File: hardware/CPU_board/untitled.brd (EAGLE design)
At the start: 128.9 x 94.9 mm, 71 parts, among them IC1 MAX232ECWE, IC2 MAX232ECWE, IC3 AM29F040J, IC4 74HCT138D, IC5 LM2596S, IC6 74245SSOP, IC7 74245SSOP, IC8 74245SSOP, J2 POWER_JACKSLT, U1 AS6C4008-55SIN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

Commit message: Minor changes
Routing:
- net GND: track 94.2 -> 95.9 mm
- net SLCT: track 92.5 -> 91.0 mm
- net PE: track 88.7 -> 87.2 mm
- net BUSY: track 85.0 -> 83.5 mm
- net /ERR: track 65.9 -> 64.4 mm
- net /ACK: track 82.2 -> 80.7 mm
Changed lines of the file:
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@@
 <contactref element="IC8" pad="4"/>
 <wire x1="72.707" y1="50.038" x2="72.707" y2="51.244" width="0.3048" layer="1"/>
-<wire x1="72.707" y1="51.244" x2="72.7202" y2="51.2572" width="0.3048" layer="1"/>
 <wire x1="72.707" y1="50.038" x2="72.707" y2="48.958" width="0.3048" layer="1"/>
 <wire x1="72.707" y1="48.958" x2="72.6948" y2="48.9458" width="0.3048" layer="1"/>
@@
 <contactref element="C26" pad="2"/>
 <contactref element="C27" pad="2"/>
+<wire x1="72.707" y1="51.244" x2="72.707" y2="51.372" width="0.2667" layer="1"/>
+<wire x1="72.707" y1="51.372" x2="72.4408" y2="51.6382" width="0.2667" layer="1"/>
+<wire x1="72.4408" y1="51.6382" x2="71.2724" y2="51.6382" width="0.2667" layer="1"/>
+<wire x1="71.2724" y1="51.6382" x2="71.247" y2="51.6636" width="0.2667" layer="1"/>
 </signal>
 <signal name="5V">
@@
 <wire x1="27.305" y1="69.85" x2="31.3182" y2="69.85" width="0.8128" layer="1"/>
 <contactref element="JP7" pad="1"/>
-<wire x1="45.2558" y1="85.9102" x2="59.69" y2="85.9102" width="1.0668" layer="1"/>
+<wire x1="45.2558" y1="85.9102" x2="59.69" y2="85.9102" width="1.6764" layer="1"/>
 <wire x1="59.69" y1="85.9102" x2="59.69" y2="88.265" width="1.0668" layer="1"/>
 <contactref element="C22" pad="+"/>
@@
 <contactref element="JP9" pad="4"/>
 <contactref element="IC8" pad="5"/>
-<wire x1="70.802" y1="56.642" x2="70.802" y2="60.3118" width="0.3048" layer="1"/>
-<wire x1="70.802" y1="60.3118" x2="71.6534" y2="61.1632" width="0.3048" layer="1"/>
-<wire x1="71.6534" y1="61.1632" x2="89.7636" y2="61.1632" width="0.3048" layer="1"/>
+<wire x1="70.802" y1="56.642" x2="70.802" y2="57.7718" width="0.3048" layer="1"/>
+<wire x1="70.802" y1="57.7718" x2="74.1934" y2="61.1632" width="0.3048" layer="1"/>
+<wire x1="74.1934" y1="61.1632" x2="89.7636" y2="61.1632" width="0.3048" layer="1"/>
 <wire x1="89.7636" y1="61.1632" x2="102.0064" y2="73.406" width="0.3048" layer="1"/>
 <wire x1="93.98" y1="76.2" x2="93.98" y2="78.105" width="0.3048" layer="1"/>
@@
 <contactref element="JP9" pad="19"/>
 <contactref element="IC8" pad="9"/>
-<wire x1="68.262" y1="56.642" x2="68.262" y2="61.2262" width="0.3048" layer="1"/>
-<wire x1="68.262" y1="61.2262" x2="70.6374" y2="63.6016" width="0.3048" layer="1"/>
-<wire x1="70.6374" y1="63.6016" x2="88.7984" y2="63.6016" width="0.3048" layer="1"/>
+<wire x1="68.262" y1="56.642" x2="68.262" y2="58.6862" width="0.3048" layer="1"/>
+<wire x1="68.262" y1="58.6862" x2="73.1774" y2="63.6016" width="0.3048" layer="1"/>
+<wire x1="73.1774" y1="63.6016" x2="88.7984" y2="63.6016" width="0.3048" layer="1"/>
 <wire x1="88.7984" y1="63.6016" x2="99.0092" y2="73.8124" width="0.3048" layer="1"/>
 <wire x1="99.0092" y1="73.8124" x2="99.0092" y2="85.0138" width="0.3048" layer="1"/>
@@
 <contactref element="JP9" pad="21"/>
 <contactref element="IC8" pad="8"/>
-<wire x1="68.897" y1="56.642" x2="68.897" y2="60.9976" width="0.3048" layer="1"/>
-<wire x1="68.897" y1="60.9976" x2="70.8914" y2="62.992" width="0.3048" layer="1"/>
-<wire x1="70.8914" y1="62.992" x2="89.027" y2="62.992" width="0.3048" layer="1"/>
+<wire x1="68.897" y1="56.642" x2="68.897" y2="58.4576" width="0.3048" layer="1"/>
+<wire x1="68.897" y1="58.4576" x2="73.4314" y2="62.992" width="0.3048" layer="1"/>
+<wire x1="73.4314" y1="62.992" x2="89.027" y2="62.992" width="0.3048" layer="1"/>
 <wire x1="89.027" y1="62.992" x2="99.6188" y2="73.5838" width="0.3048" layer="1"/>
 <wire x1="99.6188" y1="73.5838" x2="99.6188" y2="85.2678" width="0.3048" layer="1"/>
@@
 <contactref element="JP9" pad="23"/>
 <contactref element="IC8" pad="7"/>
-<wire x1="69.532" y1="56.642" x2="69.532" y2="60.769" width="0.3048" layer="1"/>
-<wire x1="69.532" y1="60.769" x2="71.1454" y2="62.3824" width="0.3048" layer="1"/>
-<wire x1="71.1454" y1="62.3824" x2="89.2556" y2="62.3824" width="0.3048" layer="1"/>
+<wire x1="69.532" y1="56.642" x2="69.532" y2="58.229" width="0.3048" layer="1"/>
+<wire x1="69.532" y1="58.229" x2="73.6854" y2="62.3824" width="0.3048" layer="1"/>
+<wire x1="73.6854" y1="62.3824" x2="89.2556" y2="62.3824" width="0.3048" layer="1"/>
 <wire x1="89.2556" y1="62.3824" x2="100.2284" y2="73.3552" width="0.3048" layer="1"/>
 <wire x1="100.2284" y1="73.3552" x2="100.2284" y2="85.5218" width="0.3048" layer="1"/>
@@
 <contactref element="JP9" pad="25"/>
 <contactref element="IC8" pad="6"/>
-<wire x1="70.167" y1="56.642" x2="70.167" y2="60.5404" width="0.3048" layer="1"/>
-<wire x1="70.167" y1="60.5404" x2="71.3994" y2="61.7728" width="0.3048" layer="1"/>
-<wire x1="71.3994" y1="61.7728" x2="89.5096" y2="61.7728" width="0.3048" layer="1"/>
+<wire x1="70.167" y1="56.642" x2="70.167" y2="58.0004" width="0.3048" layer="1"/>
+<wire x1="70.167" y1="58.0004" x2="73.9394" y2="61.7728" width="0.3048" layer="1"/>
+<wire x1="73.9394" y1="61.7728" x2="89.5096" y2="61.7728" width="0.3048" layer="1"/>
 <wire x1="89.5096" y1="61.7728" x2="100.838" y2="73.1012" width="0.3048" layer="1"/>
 <wire x1="100.838" y1="73.1012" x2="100.838" y2="85.7758" width="0.3048" layer="1"/>

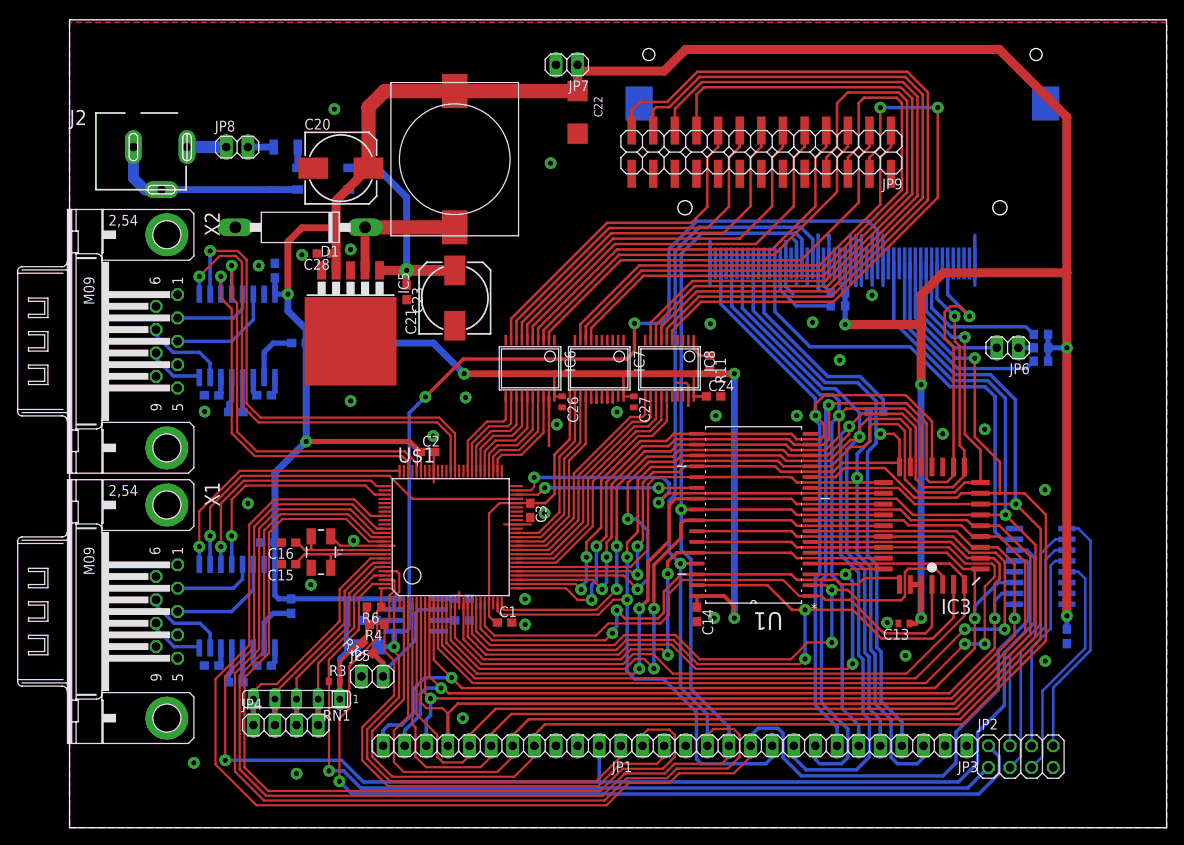
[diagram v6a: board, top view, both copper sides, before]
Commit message: Mounting holes added, board size adjusted
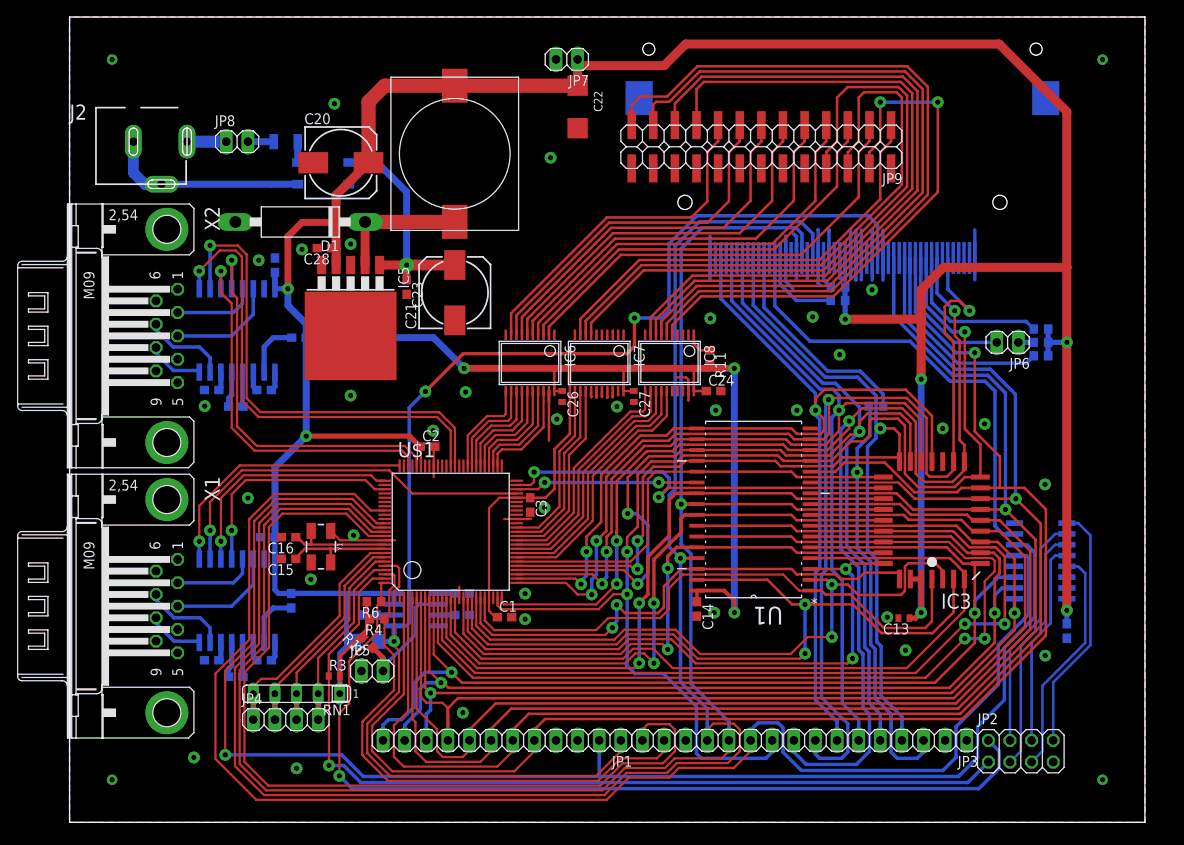
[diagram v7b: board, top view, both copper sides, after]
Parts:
- moved B1 0.64 mm to (29.8, 76.3)
- moved C2 0.64 mm to (42.1, 44.1)
- moved C20 0.64 mm to (31.9, 77.5)
- moved C24 0.64 mm to (75.7, 50.7)
- moved C28 0.64 mm to (29.9, 67.5)
- moved C9 0.64 mm to (26.9, 56.9)
- moved CON1 0.64 mm to (90.8, 85.1)
- moved F1 0.64 mm to (25.4, 80.0)
- moved IC3 0.64 mm to (101.3, 35.5)
- moved JP7 0.64 mm to (58.4, 89.6)
- moved JP8 0.64 mm to (19.7, 80.0)
- moved JP9 0.64 mm to (95.2, 78.1)
- moved R12 0.64 mm to (90.3, 61.3)
- moved R2 0.64 mm to (94.7, 48.9)
- moved R7 0.64 mm to (90.3, 62.9)
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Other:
- board size 128.9 x 94.9 mm -> 126.3 x 94.6 mm

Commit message: Dangling signals fixed
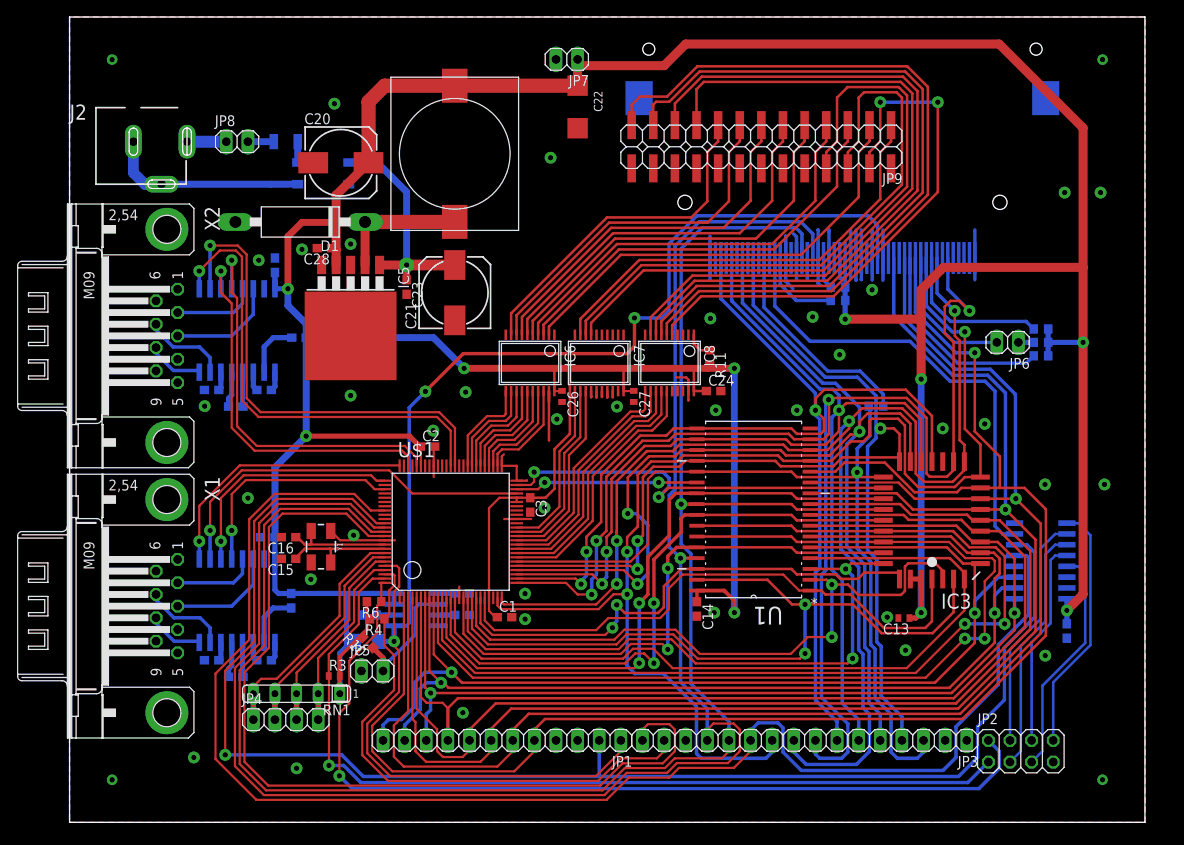
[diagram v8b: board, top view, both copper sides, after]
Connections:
- net 5V: now also U$1.45
- net GND: now also U$1.50, U$1.51
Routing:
- net GND: track 95.9 -> 102.1 mm, vias 33 -> 36
- net 5V: track 509.8 -> 515.7 mm
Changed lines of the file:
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@@
 <setting verticaltext="up"/>
 </settings>
-<grid distance="25" unitdist="mil" unit="mil" style="lines" multiple="1" display="no" altdistance="1" altunitdist="mm" altunit="mm"/>
+<grid distance="25" unitdist="mil" unit="mil" style="lines" multiple="1" display="no" altdistance="1" altunitdist="mil" altunit="mil"/>
 <layers>
 <layer number="1" name="Top" color="4" fill="1" visible="yes" active="yes"/>
@@
 <wire x1="72.4408" y1="52.2732" x2="71.2724" y2="52.2732" width="0.2667" layer="1"/>
 <wire x1="71.2724" y1="52.2732" x2="71.247" y2="52.2986" width="0.2667" layer="1"/>
+<via x="116.9162" y="73.9902" extent="1-16" drill="0.6" diameter="1.4224" shape="octagon"/>
+<via x="121.1326" y="73.9902" extent="1-16" drill="0.6" diameter="1.4224" shape="octagon"/>
+<via x="121.5898" y="39.7002" extent="1-16" drill="0.6" diameter="1.4224" shape="octagon"/>
+<contactref element="U$1" pad="50"/>
+<contactref element="U$1" pad="51"/>
+<wire x1="50.7802" y1="41.8876" x2="50.7802" y2="42.9824" width="0.2667" layer="1"/>
+<wire x1="50.7802" y1="42.9824" x2="51.0286" y2="43.2308" width="0.2667" layer="1"/>
+<wire x1="52.5302" y1="40.1376" x2="53.7012" y2="40.1376" width="0.2667" layer="1"/>
+<wire x1="53.7012" y1="40.1376" x2="53.7464" y2="40.1828" width="0.2667" layer="1"/>
+<wire x1="50.7802" y1="41.8876" x2="52.5302" y2="41.8876" width="0.2667" layer="1"/>
+<wire x1="52.5302" y1="41.8876" x2="52.5302" y2="40.1376" width="0.2667" layer="1"/>
 </signal>
 <signal name="5V">
@@
 <wire x1="117.1702" y1="24.892" x2="117.1702" y2="26.2636" width="0.6096" layer="16"/>
 <wire x1="117.1702" y1="24.892" x2="117.1702" y2="23.329" width="0.6096" layer="16"/>
-<wire x1="117.1702" y1="24.892" x2="117.1702" y2="56.388" width="1.0668" layer="1"/>
 <contactref element="R4" pad="2"/>
 <contactref element="R5" pad="2"/>
@@
 <wire x1="34.146159375" y1="21.733840625" x2="34.0741" y2="21.8059" width="0.2667" layer="1"/>
 <wire x1="31.75" y1="15.113" x2="31.75" y2="15.24" width="0.4064" layer="16"/>
-<via x="117.1702" y="56.388" extent="1-16" drill="0.6" diameter="1.4224" shape="octagon"/>
-<wire x1="114.9722" y1="56.388" x2="117.1702" y2="56.388" width="0.6096" layer="16"/>
+<via x="119.0752" y="56.388" extent="1-16" drill="0.6" diameter="1.4224" shape="octagon"/>
+<wire x1="114.9722" y1="56.388" x2="119.0752" y2="56.388" width="0.6096" layer="16"/>
 <contactref element="C20" pad="+"/>
 <wire x1="31.3182" y1="65.4812" x2="31.3182" y2="67.31" width="1.0668" layer="1"/>
@@
 <wire x1="41.2124" y1="44.1452" x2="41.1734" y2="44.1452" width="0.6096" layer="1"/>
 <via x="91.1216" y="59.1194" extent="1-16" drill="0.6" diameter="1.4224" shape="octagon"/>
-<wire x1="109.22" y1="91.44" x2="117.1702" y2="83.4898" width="1.0668" layer="1"/>
-<wire x1="117.1702" y1="56.388" x2="117.1702" y2="65.20024375" width="1.0668" layer="1"/>
-<wire x1="117.1702" y1="65.20024375" x2="117.1702" y2="83.4898" width="1.0668" layer="1"/>
+<wire x1="109.22" y1="91.44" x2="119.0752" y2="81.5848" width="1.0668" layer="1"/>
+<wire x1="119.0752" y1="56.388" x2="119.0752" y2="65.20024375" width="1.0668" layer="1"/>
+<wire x1="119.0752" y1="65.20024375" x2="119.0752" y2="81.5848" width="1.0668" layer="1"/>
 <wire x1="91.1216" y1="59.1194" x2="100.0506" y2="59.1194" width="1.0668" layer="1"/>
 <wire x1="100.0506" y1="59.1194" x2="100.0506" y2="52.07" width="1.0668" layer="1"/>
-<wire x1="117.1702" y1="65.20024375" x2="102.66524375" y2="65.20024375" width="1.0668" layer="1"/>
+<wire x1="119.0752" y1="65.20024375" x2="102.66524375" y2="65.20024375" width="1.0668" layer="1"/>
 <wire x1="102.66524375" y1="65.20024375" x2="100.0506" y2="62.5856" width="1.0668" layer="1"/>
 <wire x1="100.0506" y1="59.1194" x2="100.0506" y2="62.5856" width="1.0668" layer="1"/>
@@
 <wire x1="56.959" y1="50.673" x2="57.8462" y2="50.673" width="0.2667" layer="1"/>
 <wire x1="57.8462" y1="50.673" x2="57.8612" y2="50.688" width="0.2667" layer="1"/>
+<wire x1="119.0752" y1="56.388" x2="119.0752" y2="26.797" width="1.0668" layer="1"/>
+<wire x1="119.0752" y1="26.797" x2="117.1702" y2="24.892" width="1.0668" layer="1"/>
+<contactref element="U$1" pad="45"/>
+<wire x1="52.5302" y1="37.6376" x2="52.5302" y2="38.1376" width="0.2667" layer="1"/>
 <wire x1="59.69" y1="86.5452" x2="59.69" y2="86.5486" width="0" layer="19" extent="1-1"/>
 <wire x1="59.69" y1="9.6266" x2="50.2548" y2="24.1046" width="0" layer="19" extent="1-1"/>
@@
 <contactref element="IC6" pad="18"/>
 <wire x1="50.2802" y1="43.2952" x2="50.8" y2="43.815" width="0.2667" layer="1"/>
-<wire x1="50.8" y1="43.815" x2="53.086" y2="43.815" width="0.2667" layer="1"/>
-<wire x1="53.086" y1="43.815" x2="55.689" y2="46.418" width="0.2667" layer="1"/>
-<wire x1="55.689" y1="50.673" x2="55.689" y2="46.418" width="0.2667" layer="1"/>
+<wire x1="50.8" y1="43.815" x2="52.7812" y2="43.815" width="0.2667" layer="1"/>
+<wire x1="55.689" y1="50.673" x2="55.689" y2="46.7228" width="0.2667" layer="1"/>
+<wire x1="55.689" y1="46.7228" x2="52.7812" y2="43.815" width="0.2667" layer="1"/>
 </signal>
 <signal name="PD1_IN">
@@
 <contactref element="IC6" pad="17"/>
 <wire x1="49.7802" y1="43.608" x2="50.546" y2="44.3738" width="0.2667" layer="1"/>
-<wire x1="50.546" y1="44.3738" x2="52.832" y2="44.3738" width="0.2667" layer="1"/>
-<wire x1="52.832" y1="44.3738" x2="55.054" y2="46.5958" width="0.2667" layer="1"/>
-<wire x1="55.054" y1="50.673" x2="55.054" y2="46.5958" width="0.2667" layer="1"/>
+<wire x1="50.546" y1="44.3738" x2="52.5272" y2="44.3738" width="0.2667" layer="1"/>
+<wire x1="55.054" y1="50.673" x2="55.054" y2="46.9006" width="0.2667" layer="1"/>
+<wire x1="55.054" y1="46.9006" x2="52.5272" y2="44.3738" width="0.2667" layer="1"/>
 </signal>
 <signal name="PD2_IN">
@@
 <wire x1="49.2802" y1="41.8876" x2="49.2802" y2="43.9208" width="0.2667" layer="1"/>
 <wire x1="49.2802" y1="43.9208" x2="50.292" y2="44.9326" width="0.2667" layer="1"/>
-<wire x1="50.292" y1="44.9326" x2="52.578" y2="44.9326" width="0.2667" layer="1"/>
-<wire x1="52.578" y1="44.9326" x2="54.419" y2="46.7736" width="0.2667" layer="1"/>
-<wire x1="54.419" y1="50.673" x2="54.419" y2="46.7736" width="0.2667" layer="1"/>
+<wire x1="50.292" y1="44.9326" x2="52.2732" y2="44.9326" width="0.2667" layer="1"/>
+<wire x1="54.419" y1="50.673" x2="54.419" y2="47.0784" width="0.2667" layer="1"/>
+<wire x1="54.419" y1="47.0784" x2="52.2732" y2="44.9326" width="0.2667" layer="1"/>
 </signal>
 <signal name="PD3_IN">
@@
 <wire x1="48.7802" y1="41.8876" x2="48.7802" y2="44.2336" width="0.2667" layer="1"/>
 <wire x1="48.7802" y1="44.2336" x2="50.038" y2="45.4914" width="0.2667" layer="1"/>
-<wire x1="50.038" y1="45.4914" x2="52.324" y2="45.4914" width="0.2667" layer="1"/>
-<wire x1="52.324" y1="45.4914" x2="53.784" y2="46.9514" width="0.2667" layer="1"/>
-<wire x1="53.784" y1="50.673" x2="53.784" y2="46.9514" width="0.2667" layer="1"/>
+<wire x1="50.038" y1="45.4914" x2="52.0192" y2="45.4914" width="0.2667" layer="1"/>
+<wire x1="53.784" y1="50.673" x2="53.784" y2="47.2562" width="0.2667" layer="1"/>
+<wire x1="53.784" y1="47.2562" x2="52.0192" y2="45.4914" width="0.2667" layer="1"/>
 </signal>
 <signal name="PD4_IN">
@@
 <contactref element="IC6" pad="14"/>
 <wire x1="48.2802" y1="44.5464" x2="49.784" y2="46.0502" width="0.2667" layer="1"/>
-<wire x1="49.784" y1="46.0502" x2="52.0192" y2="46.0502" width="0.2667" layer="1"/>
-<wire x1="52.0192" y1="46.0502" x2="53.149" y2="47.18" width="0.2667" layer="1"/>
-<wire x1="53.149" y1="50.673" x2="53.149" y2="47.18" width="0.2667" layer="1"/>
+<wire x1="53.149" y1="50.673" x2="53.149" y2="47.434" width="0.2667" layer="1"/>
+<wire x1="49.784" y1="46.0502" x2="51.7652" y2="46.0502" width="0.2667" layer="1"/>
+<wire x1="53.149" y1="47.434" x2="51.7652" y2="46.0502" width="0.2667" layer="1"/>
 </signal>
 <signal name="PD5_IN">
@@
 <wire x1="47.7802" y1="41.8876" x2="47.7802" y2="44.8592" width="0.2667" layer="1"/>
 <wire x1="47.7802" y1="44.8592" x2="49.53" y2="46.609" width="0.2667" layer="1"/>
-<wire x1="49.53" y1="46.609" x2="51.7652" y2="46.609" width="0.2667" layer="1"/>
-<wire x1="51.7652" y1="46.609" x2="52.514" y2="47.3578" width="0.2667" layer="1"/>
-<wire x1="52.514" y1="50.673" x2="52.514" y2="47.3578" width="0.2667" layer="1"/>
+<wire x1="49.53" y1="46.609" x2="51.5112" y2="46.609" width="0.2667" layer="1"/>
+<wire x1="52.514" y1="50.673" x2="52.514" y2="47.6118" width="0.2667" layer="1"/>
+<wire x1="52.514" y1="47.6118" x2="51.5112" y2="46.609" width="0.2667" layer="1"/>
 </signal>
 <signal name="PD6_IN">
@@
 <wire x1="47.2802" y1="41.8876" x2="47.2802" y2="45.172" width="0.2667" layer="1"/>
 <wire x1="47.2802" y1="45.172" x2="49.276" y2="47.1678" width="0.2667" layer="1"/>
-<wire x1="49.276" y1="47.1678" x2="51.5112" y2="47.1678" width="0.2667" layer="1"/>
-<wire x1="51.5112" y1="47.1678" x2="51.879" y2="47.5356" width="0.2667" layer="1"/>
-<wire x1="51.879" y1="50.673" x2="51.879" y2="47.5356" width="0.2667" layer="1"/>
+<wire x1="49.276" y1="47.1678" x2="51.2572" y2="47.1678" width="0.2667" layer="1"/>
+<wire x1="51.879" y1="50.673" x2="51.879" y2="47.7896" width="0.2667" layer="1"/>
+<wire x1="51.879" y1="47.7896" x2="51.2572" y2="47.1678" width="0.2667" layer="1"/>
 </signal>
 <signal name="PD7_IN">
